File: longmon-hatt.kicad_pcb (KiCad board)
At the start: 2 copper layers, 67.5 x 36 mm, 4 parts

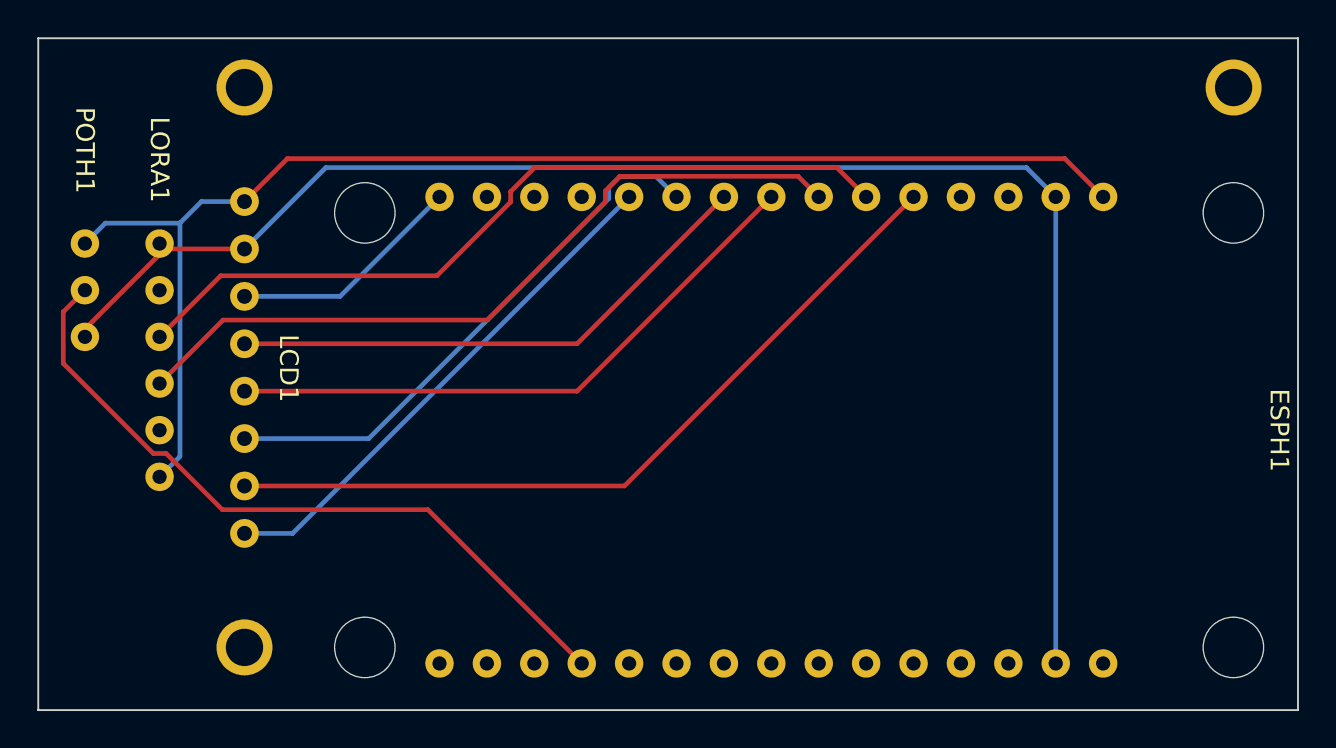
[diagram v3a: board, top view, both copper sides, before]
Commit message: Replace ESP32 with imported library
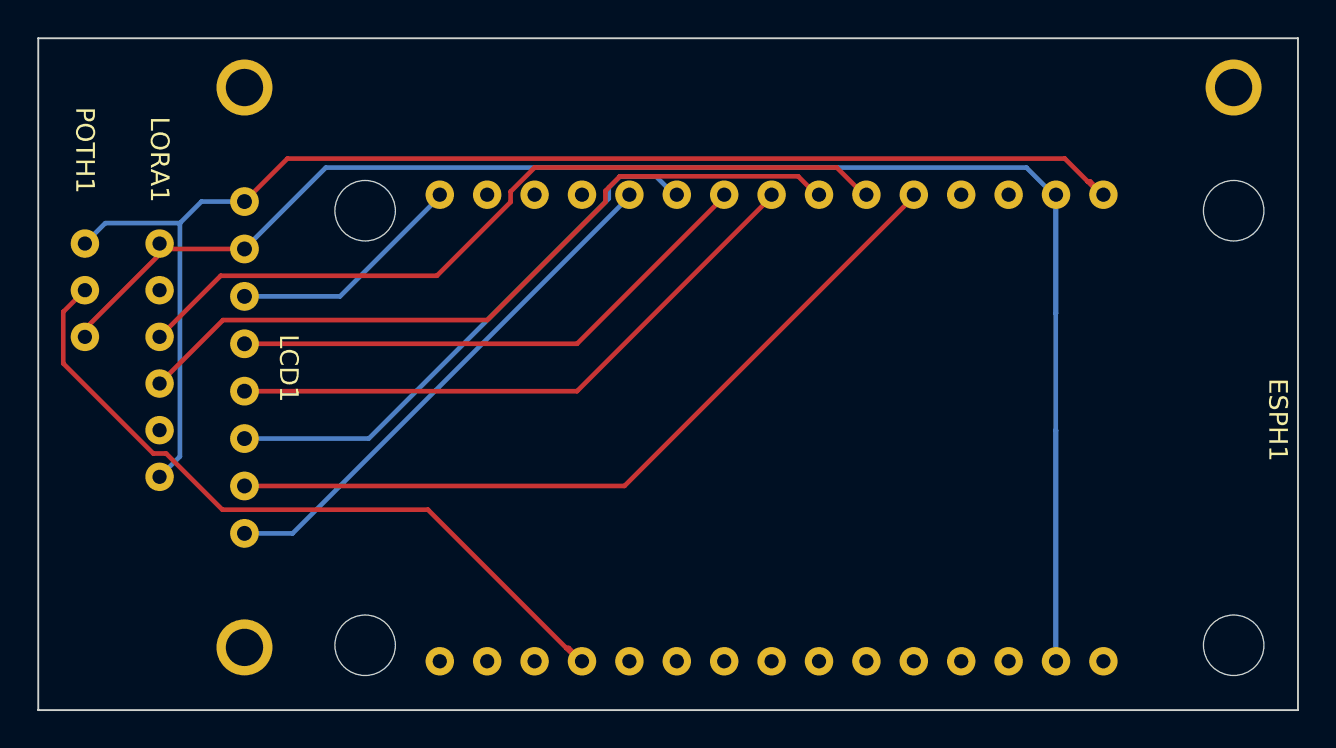
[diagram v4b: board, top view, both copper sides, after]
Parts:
- moved ESPH1 0.12 mm to (150.0, 112.4)
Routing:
- net Net-(LCD1-GND): track 82.1 -> 100.8 mm
- net Net-(ESPH1-D34): track 38.8 -> 40.0 mm
- net Net-(LCD1-VCC): track 71.3 -> 72.5 mm
- net Net-(ESPH1-D19): track 29.8 -> 30.5 mm
